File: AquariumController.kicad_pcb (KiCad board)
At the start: 2 copper layers, 58.4 x 132.1 mm, 16 parts, among them J1 Temp_1_Screw_Terminal, J2 Temp_2_Screw_Terminal, J3 12V_Output_1_Screw_Terminal, J4 12V_Output_2_Screw_Terminal, J5 Input_1_Screw_Terminal, J6 Input_2_Screw_Terminal, J7 IR_LED_Screw_Terminal, J8 Conn_01x02, Q1 IRF3708, Q2 IRF3708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

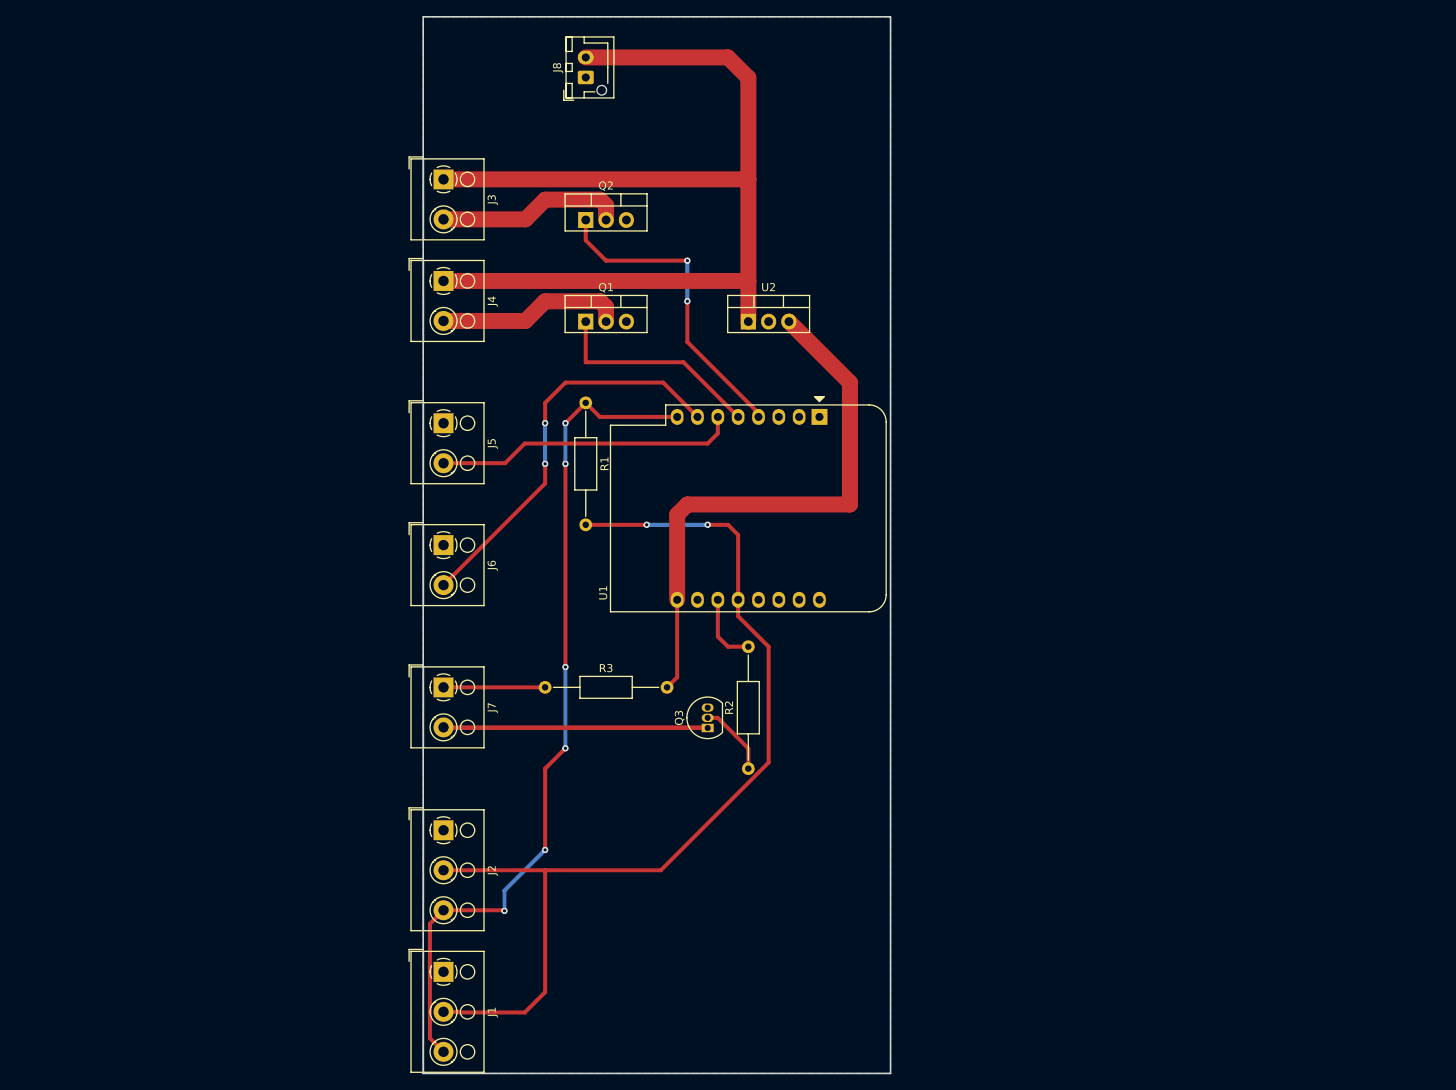
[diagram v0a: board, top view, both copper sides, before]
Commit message: Swap out all the mosfets/bjts add the i2c breakout flip the power to the right side
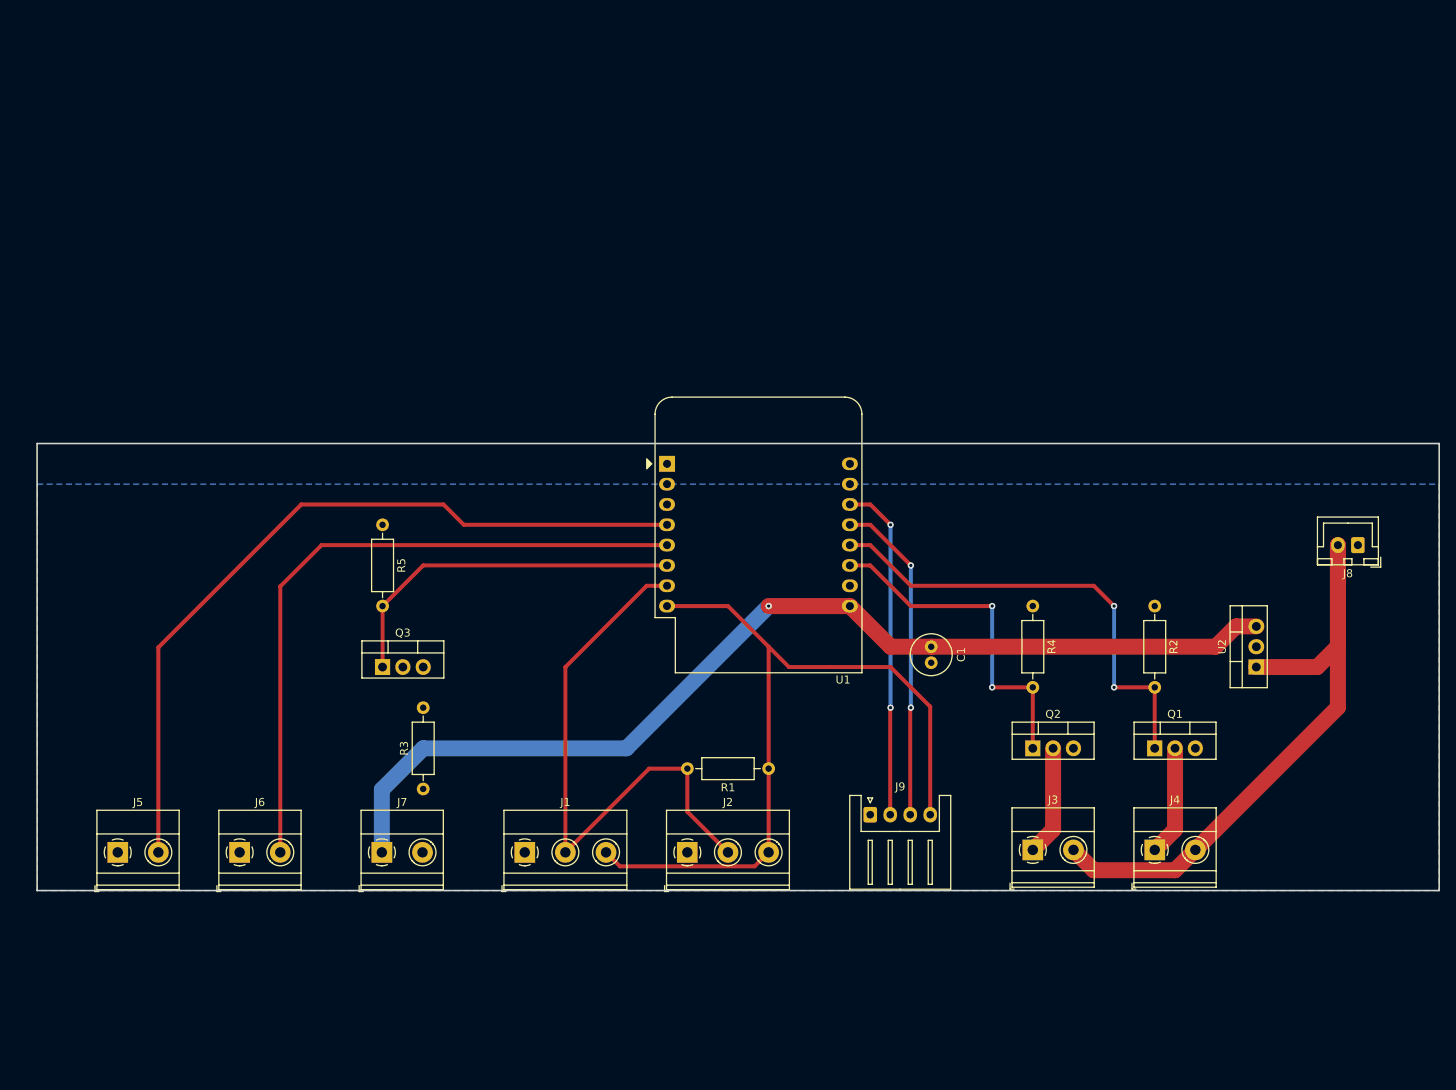
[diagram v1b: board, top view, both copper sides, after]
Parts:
- added C1: C_Polarized, Capacitor_THT:C_Radial_D5.0mm_H11.0mm_P2.00mm, F.Cu at (139.7, 104.1)
- added J9: I2C, Connector_JST:JST_XH_S4B-XH-A_1x04_P2.50mm_Horizontal, F.Cu at (132.1, 125.1)
- added R4: 100k, Resistor_THT:R_Axial_DIN0207_L6.3mm_D2.5mm_P10.16mm_Horizontal, F.Cu at (152.4, 99.1)
- added R5: 100k, Resistor_THT:R_Axial_DIN0207_L6.3mm_D2.5mm_P10.16mm_Horizontal, F.Cu at (71.1, 88.9)
- J1: value Temp_1_Screw_Terminal -> Temp_1; footprint TerminalBlock_RND:TerminalBlock_RND_205-00002_1x03_P5.00mm_Horizontal -> TerminalBlock_Phoenix:TerminalBlock_Phoenix_MKDS-1,5-3-5.08_1x03_P5.08mm_Horizontal
- J2: value Temp_2_Screw_Terminal -> Temp_2; footprint TerminalBlock_RND:TerminalBlock_RND_205-00002_1x03_P5.00mm_Horizontal -> TerminalBlock_Phoenix:TerminalBlock_Phoenix_MKDS-1,5-3-5.08_1x03_P5.08mm_Horizontal
- J3: value 12V_Output_1_Screw_Terminal -> 12V_Output_1; footprint TerminalBlock_RND:TerminalBlock_RND_205-00001_1x02_P5.00mm_Horizontal -> TerminalBlock_Phoenix:TerminalBlock_Phoenix_MKDS-1,5-2-5.08_1x02_P5.08mm_Horizontal
- J4: value 12V_Output_2_Screw_Terminal -> 12V_Output_2; footprint TerminalBlock_RND:TerminalBlock_RND_205-00001_1x02_P5.00mm_Horizontal -> TerminalBlock_Phoenix:TerminalBlock_Phoenix_MKDS-1,5-2-5.08_1x02_P5.08mm_Horizontal
- J5: value Input_1_Screw_Terminal -> Input_1; footprint TerminalBlock_RND:TerminalBlock_RND_205-00001_1x02_P5.00mm_Horizontal -> TerminalBlock_Phoenix:TerminalBlock_Phoenix_MKDS-1,5-2-5.08_1x02_P5.08mm_Horizontal
- J6: value Input_2_Screw_Terminal -> Input_2; footprint TerminalBlock_RND:TerminalBlock_RND_205-00001_1x02_P5.00mm_Horizontal -> TerminalBlock_Phoenix:TerminalBlock_Phoenix_MKDS-1,5-2-5.08_1x02_P5.08mm_Horizontal
- J7: value IR_LED_Screw_Terminal -> IR_LED; footprint TerminalBlock_RND:TerminalBlock_RND_205-00001_1x02_P5.00mm_Horizontal -> TerminalBlock_Phoenix:TerminalBlock_Phoenix_MKDS-1,5-2-5.08_1x02_P5.08mm_Horizontal
- J8: footprint Connector_JST:JST_XH_B2B-XH-AM_1x02_P2.50mm_Vertical -> Connector_JST:JST_XH_B2B-XH-A_1x02_P2.50mm_Vertical
- Q1, Q2: value IRF3708 -> IRLB8721PBF
- Q3: value BC547 -> IRLB8721PBF; footprint Package_TO_SOT_THT:TO-92_Inline -> Package_TO_SOT_THT:TO-220-3_Vertical
- R1, R3: footprint Resistor_THT:R_Axial_DIN0207_L6.3mm_D2.5mm_P15.24mm_Horizontal -> Resistor_THT:R_Axial_DIN0207_L6.3mm_D2.5mm_P10.16mm_Horizontal
- R2: value 1k -> 100k; footprint Resistor_THT:R_Axial_DIN0207_L6.3mm_D2.5mm_P15.24mm_Horizontal -> Resistor_THT:R_Axial_DIN0207_L6.3mm_D2.5mm_P10.16mm_Horizontal
- moved J4 113.8 mm to (167.6, 129.5), turned to 0 degrees
- moved J8 112.8 mm to (193.0, 91.4), turned to 180 degrees
- moved J3 111.6 mm to (152.4, 129.5), turned to 0 degrees
- moved Q1 88.9 mm to (167.6, 116.8)
- moved Q2 86.5 mm to (152.4, 116.8)
- moved U2 76.8 mm to (180.3, 106.7), turned to 90 degrees
- moved J5 67.4 mm to (38.0, 129.8), turned to 0 degrees
- moved R2 54.7 mm to (167.6, 99.1), turned to -90 degrees
- moved R1 51.1 mm to (119.4, 119.4), turned to 180 degrees
- moved J6 46.1 mm to (53.3, 129.8), turned to 0 degrees
- moved Q3 41.3 mm to (71.1, 106.7), turned to 0 degrees
- moved J2 30.6 mm to (109.2, 129.8), turned to 0 degrees
- moved J7 22.0 mm to (71.0, 129.8), turned to 0 degrees
- moved U1 19.9 mm to (106.7, 81.3), turned to 0 degrees
- moved R3 19.8 mm to (76.2, 121.9), turned to 90 degrees
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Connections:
- J1 pad 2: Net-(R1-Pad2) -> /D8
- J2 pad 2: Net-(R1-Pad2) -> /D8
- J3 pad 1: +12V -> Net-(Q2-Pad2)
- J3 pad 2: Net-(J3-Pad2) -> +12V
- J4 pad 1: +12V -> Net-(Q1-Pad2)
- J4 pad 2: Net-(J4-Pad2) -> +12V
- J5 pad 2: Net-(U1-Pad6) -> /D5
- J6 pad 2: Net-(U1-Pad7) -> /D6
- J7 pad 1: Net-(J7-Pad1) -> /5v
- Q1 pad 1: Net-(U1-Pad5) -> /D3
- Q1 pad 2: Net-(J4-Pad2) -> Net-(Q1-Pad2)
- Q2 pad 1: Net-(U1-Pad4) -> /D4
- Q2 pad 2: Net-(J3-Pad2) -> Net-(Q2-Pad2)
- Q3 pad 1: Net-(J7-Pad2) -> /D7
- R1 pad 2: Net-(R1-Pad2) -> /D8
- R2 pad 1: Net-(Q3-Pad2) -> GND
- R2 pad 2: Net-(U1-Pad11) -> /D3
- R3 pad 1: Net-(J7-Pad1) -> Net-(J7-Pad2)
- R3 pad 2: /5v -> Net-(Q3-Pad2)
- U1 pad 11: Net-(U1-Pad11) -> /D4
- U1 pad 12: Net-(R1-Pad2) -> /D3
- U1 pad 13: unconnected-(U1-Pad13) -> /SDA
- U1 pad 14: unconnected-(U1-Pad14) -> /SCL
- U1 pad 4: Net-(U1-Pad4) -> /D5
- U1 pad 5: Net-(U1-Pad5) -> /D6
- U1 pad 6: Net-(U1-Pad6) -> /D7
- U1 pad 7: Net-(U1-Pad7) -> /D8
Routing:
- net Net-(R1-Pad2): track 124.8 -> 0.00 mm, vias 2 -> 0
- net /D5: track 0.00 -> 97.7 mm
- net /D6: track 0.00 -> 83.7 mm
- net /D8: track 0.00 -> 72.2 mm
- net Net-(J7-Pad2): track 66.1 -> 0.00 mm
- net /5v: track 70.2 -> 129.8 mm, vias 0 -> 1
- net /D3: track 0.00 -> 59.0 mm, vias 0 -> 2
- net Net-(U1-Pad7): track 49.9 -> 0.00 mm, vias 2 -> 0
- net /D7: track 0.00 -> 45.3 mm
- net /D4: track 0.00 -> 42.7 mm, vias 0 -> 2
- net /SCL: track 0.00 -> 42.4 mm, vias 0 -> 2
- net +12V: track 128.1 -> 86.8 mm
- net /SDA: track 0.00 -> 40.9 mm, vias 0 -> 2
- net Net-(U1-Pad4): track 39.5 -> 0.00 mm, vias 2 -> 0
- net Net-(U1-Pad6): track 37.9 -> 0.00 mm
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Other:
- board size 58.4 x 132.1 mm -> 175.3 x 55.9 mm

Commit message: tweaks
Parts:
- added ?: M3, MountingHole:MountingHole_3.2mm_M3_Pad_Via, F.Cu at (30.5, 76.2)
- added ?: M3, MountingHole:MountingHole_3.2mm_M3_Pad_Via, F.Cu at (198.1, 76.2)
- added ?: M3, MountingHole:MountingHole_3.2mm_M3_Pad_Via, F.Cu at (198.1, 129.5)
- added ?: M3, MountingHole:MountingHole_3.2mm_M3_Pad_Via, F.Cu at (30.5, 129.5)
- moved J7 0.32 mm to (71.1, 129.5)
- moved J1 0.31 mm to (88.9, 129.5)
- moved J2 0.31 mm to (109.2, 129.5)
- moved J5 0.31 mm to (38.0, 129.5)
- moved J6 0.31 mm to (53.3, 129.5)
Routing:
- net /D8: track 72.2 -> 64.3 mm
- net Net-(J7-Pad2): track 0.00 -> 7.62 mm
- net Net-(Q3-Pad2): track 0.00 -> 6.13 mm
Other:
- board size 175.3 x 55.9 mm -> 177.8 x 63.5 mm

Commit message: make the holes not on the schematic and fix the name of the 12v input
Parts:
- J8: value Conn_01x02 -> 12v Input
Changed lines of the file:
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@@
   (net 11 "/SCL")
   (net 12 "/SDA")
-  (net 13 "Net-(Q2-Pad2)")
-  (net 14 "Net-(Q1-Pad2)")
+  (net 13 "Net-(J3-Pad1)")
+  (net 14 "Net-(J4-Pad1)")
   (net 15 "Net-(Q3-Pad2)")
   (net 16 "/D8")
@@
       (effects (font (size 1 1) (thickness 0.15)))
     )
-    (fp_text value "Conn_01x02" (at 1.25 4.6) (layer "F.Fab")
+    (fp_text value "12v Input" (at 1.25 4.6) (layer "F.Fab")
       (effects (font (size 1 1) (thickness 0.15)))
     )
@@
     (descr "Mounting Hole 3.2mm, M3")
     (tags "mounting hole 3.2mm m3")
-    (attr exclude_from_pos_files exclude_from_bom)
+    (attr board_only exclude_from_pos_files exclude_from_bom)
     (fp_text reference "" (at 0 -4.2) (layer "F.SilkS")
       (effects (font (size 1 1) (thickness 0.15)))
@@
       (net 19 "/D3") (pinfunction "G") (pintype "input"))
     (pad "2" thru_hole oval (at 2.54 0) (size 1.905 2) (drill 1.1) (layers *.Cu *.Mask)
-      (net 14 "Net-(Q1-Pad2)") (pinfunction "D") (pintype "passive"))
+      (net 14 "Net-(J4-Pad1)") (pinfunction "D") (pintype "passive"))
     (pad "3" thru_hole oval (at 5.08 0) (size 1.905 2) (drill 1.1) (layers *.Cu *.Mask)
       (net 1 "GND") (pinfunction "S") (pintype "passive"))
@@
       (net 20 "/D4") (pinfunction "G") (pintype "input"))
     (pad "2" thru_hole oval (at 2.54 0) (size 1.905 2) (drill 1.1) (layers *.Cu *.Mask)
-      (net 13 "Net-(Q2-Pad2)") (pinfunction "D") (pintype "passive"))
+      (net 13 "Net-(J3-Pad1)") (pinfunction "D") (pintype "passive"))
     (pad "3" thru_hole oval (at 5.08 0) (size 1.905 2) (drill 1.1) (layers *.Cu *.Mask)
       (net 1 "GND") (pinfunction "S") (pintype "passive"))
@@
     (fp_circle (center 5.08 0) (end 6.58 0) (layer "F.Fab") (width 0.1) (fill none))
     (pad "1" thru_hole rect (at 0 0) (size 2.6 2.6) (drill 1.3) (layers *.Cu *.Mask)
-      (net 13 "Net-(Q2-Pad2)") (pinfunction "Pin_1") (pintype "passive"))
+      (net 13 "Net-(J3-Pad1)") (pinfunction "Pin_1") (pintype "passive"))
     (pad "2" thru_hole circle (at 5.08 0) (size 2.6 2.6) (drill 1.3) (layers *.Cu *.Mask)
       (net 10 "+12V") (pinfunction "Pin_2") (pintype "passive"))
@@
     (fp_circle (center 5.08 0) (end 6.58 0) (layer "F.Fab") (width 0.1) (fill none))
     (pad "1" thru_hole rect (at 0 0) (size 2.6 2.6) (drill 1.3) (layers *.Cu *.Mask)
-      (net 14 "Net-(Q1-Pad2)") (pinfunction "Pin_1") (pintype "passive"))
+      (net 14 "Net-(J4-Pad1)") (pinfunction "Pin_1") (pintype "passive"))
     (pad "2" thru_hole circle (at 5.08 0) (size 2.6 2.6) (drill 1.3) (layers *.Cu *.Mask)
       (net 10 "+12V") (pinfunction "Pin_2") (pintype "passive"))
@@
     (descr "Mounting Hole 3.2mm, M3")
     (tags "mounting hole 3.2mm m3")
-    (attr exclude_from_pos_files exclude_from_bom)
+    (attr board_only exclude_from_pos_files exclude_from_bom)
     (fp_text reference "" (at 0 -4.2) (layer "F.SilkS")
       (effects (font (size 1 1) (thickness 0.15)))
@@
     (fp_circle (center 0 0) (end 3.2 0) (layer "Cmts.User") (width 0.15) (fill none))
     (fp_circle (center 0 0) (end 3.45 0) (layer "F.CrtYd") (width 0.05) (fill none))
+    (pad "1" thru_hole circle (at 0 -2.4) (size 0.8 0.8) (drill 0.5) (layers *.Cu *.Mask))
     (pad "1" thru_hole circle (at 1.697056 1.697056) (size 0.8 0.8) (drill 0.5) (layers *.Cu *.Mask))
+    (pad "1" thru_hole circle (at 1.697056 -1.697056) (size 0.8 0.8) (drill 0.5) (layers *.Cu *.Mask))
+    (pad "1" thru_hole circle (at -1.697056 1.697056) (size 0.8 0.8) (drill 0.5) (layers *.Cu *.Mask))
+    (pad "1" thru_hole circle (at -2.4 0) (size 0.8 0.8) (drill 0.5) (layers *.Cu *.Mask))
+    (pad "1" thru_hole circle (at 0 0) (size 6.4 6.4) (drill 3.2) (layers *.Cu *.Mask))
     (pad "1" thru_hole circle (at -1.697056 -1.697056) (size 0.8 0.8) (drill 0.5) (layers *.Cu *.Mask))
-    (pad "1" thru_hole circle (at 0 0) (size 6.4 6.4) (drill 3.2) (layers *.Cu *.Mask))
-    (pad "1" thru_hole circle (at 1.697056 -1.697056) (size 0.8 0.8) (drill 0.5) (layers *.Cu *.Mask))
-    (pad "1" thru_hole circle (at -2.4 0) (size 0.8 0.8) (drill 0.5) (layers *.Cu *.Mask))
+    (pad "1" thru_hole circle (at 2.4 0) (size 0.8 0.8) (drill 0.5) (layers *.Cu *.Mask))
     (pad "1" thru_hole circle (at 0 2.4) (size 0.8 0.8) (drill 0.5) (layers *.Cu *.Mask))
-    (pad "1" thru_hole circle (at 0 -2.4) (size 0.8 0.8) (drill 0.5) (layers *.Cu *.Mask))
-    (pad "1" thru_hole circle (at 2.4 0) (size 0.8 0.8) (drill 0.5) (layers *.Cu *.Mask))
-    (pad "1" thru_hole circle (at -1.697056 1.697056) (size 0.8 0.8) (drill 0.5) (layers *.Cu *.Mask))
   )
   (footprint "MountingHole:MountingHole_3.2mm_M3_Pad_Via" (layer "F.Cu")
@@
     (descr "Mounting Hole 3.2mm, M3")
     (tags "mounting hole 3.2mm m3")
-    (attr exclude_from_pos_files exclude_from_bom)
+    (attr board_only exclude_from_pos_files exclude_from_bom)
     (fp_text reference "" (at 0 -4.2) (layer "F.SilkS")
       (effects (font (size 1 1) (thickness 0.15)))
@@
     (fp_circle (center 0 0) (end 3.2 0) (layer "Cmts.User") (width 0.15) (fill none))
     (fp_circle (center 0 0) (end 3.45 0) (layer "F.CrtYd") (width 0.05) (fill none))
-    (pad "1" thru_hole circle (at 1.697056 1.697056) (size 0.8 0.8) (drill 0.5) (layers *.Cu *.Mask))
     (pad "1" thru_hole circle (at -1.697056 -1.697056) (size 0.8 0.8) (drill 0.5) (layers *.Cu *.Mask))
     (pad "1" thru_hole circle (at 0 0) (size 6.4 6.4) (drill 3.2) (layers *.Cu *.Mask))
+    (pad "1" thru_hole circle (at 2.4 0) (size 0.8 0.8) (drill 0.5) (layers *.Cu *.Mask))
+    (pad "1" thru_hole circle (at -1.697056 1.697056) (size 0.8 0.8) (drill 0.5) (layers *.Cu *.Mask))
     (pad "1" thru_hole circle (at 1.697056 -1.697056) (size 0.8 0.8) (drill 0.5) (layers *.Cu *.Mask))
     (pad "1" thru_hole circle (at -2.4 0) (size 0.8 0.8) (drill 0.5) (layers *.Cu *.Mask))
+    (pad "1" thru_hole circle (at 0 -2.4) (size 0.8 0.8) (drill 0.5) (layers *.Cu *.Mask))
+    (pad "1" thru_hole circle (at 1.697056 1.697056) (size 0.8 0.8) (drill 0.5) (layers *.Cu *.Mask))
     (pad "1" thru_hole circle (at 0 2.4) (size 0.8 0.8) (drill 0.5) (layers *.Cu *.Mask))
-    (pad "1" thru_hole circle (at 0 -2.4) (size 0.8 0.8) (drill 0.5) (layers *.Cu *.Mask))
-    (pad "1" thru_hole circle (at 2.4 0) (size 0.8 0.8) (drill 0.5) (layers *.Cu *.Mask))
-    (pad "1" thru_hole circle (at -1.697056 1.697056) (size 0.8 0.8) (drill 0.5) (layers *.Cu *.Mask))
   )
   (footprint "TerminalBlock_Phoenix:TerminalBlock_Phoenix_MKDS-1,5-3-5.08_1x03_P5.08mm_Horizontal" (layer "F.Cu")
@@
     (descr "Mounting Hole 3.2mm, M3")
     (tags "mounting hole 3.2mm m3")
-    (attr exclude_from_pos_files exclude_from_bom)
+    (attr board_only exclude_from_pos_files exclude_from_bom)
     (fp_text reference "" (at 0 -4.2) (layer "F.SilkS")
       (effects (font (size 1 1) (thickness 0.15)))
@@
     (fp_circle (center 0 0) (end 3.2 0) (layer "Cmts.User") (width 0.15) (fill none))
     (fp_circle (center 0 0) (end 3.45 0) (layer "F.CrtYd") (width 0.05) (fill none))
-    (pad "1" thru_hole circle (at 1.697056 1.697056) (size 0.8 0.8) (drill 0.5) (layers *.Cu *.Mask))
-    (pad "1" thru_hole circle (at -1.697056 -1.697056) (size 0.8 0.8) (drill 0.5) (layers *.Cu *.Mask))
-    (pad "1" thru_hole circle (at 0 0) (size 6.4 6.4) (drill 3.2) (layers *.Cu *.Mask))
+    (pad "1" thru_hole circle (at -1.697056 1.697056) (size 0.8 0.8) (drill 0.5) (layers *.Cu *.Mask))
+    (pad "1" thru_hole circle (at -2.4 0) (size 0.8 0.8) (drill 0.5) (layers *.Cu *.Mask))
     (pad "1" thru_hole circle (at 1.697056 -1.697056) (size 0.8 0.8) (drill 0.5) (layers *.Cu *.Mask))
-    (pad "1" thru_hole circle (at -2.4 0) (size 0.8 0.8) (drill 0.5) (layers *.Cu *.Mask))
-    (pad "1" thru_hole circle (at 0 2.4) (size 0.8 0.8) (drill 0.5) (layers *.Cu *.Mask))
     (pad "1" thru_hole circle (at 0 -2.4) (size 0.8 0.8) (drill 0.5) (layers *.Cu *.Mask))
     (pad "1" thru_hole circle (at 2.4 0) (size 0.8 0.8) (drill 0.5) (layers *.Cu *.Mask))
-    (pad "1" thru_hole circle (at -1.697056 1.697056) (size 0.8 0.8) (drill 0.5) (layers *.Cu *.Mask))
+    (pad "1" thru_hole circle (at 0 2.4) (size 0.8 0.8) (drill 0.5) (layers *.Cu *.Mask))
+    (pad "1" thru_hole circle (at -1.697056 -1.697056) (size 0.8 0.8) (drill 0.5) (layers *.Cu *.Mask))
+    (pad "1" thru_hole circle (at 1.697056 1.697056) (size 0.8 0.8) (drill 0.5) (layers *.Cu *.Mask))
+    (pad "1" thru_hole circle (at 0 0) (size 6.4 6.4) (drill 3.2) (layers *.Cu *.Mask))
   )
   (gr_rect (start 25.4 134.62) (end 203.2 71.12) (layer "Edge.Cuts") (width 0.2) (fill none))
